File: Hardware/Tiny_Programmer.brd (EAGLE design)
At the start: 59.7 x 15.2 mm, 31 parts, among them Q1 16MHz, U1 ATTINY84, X1 USB-A-H

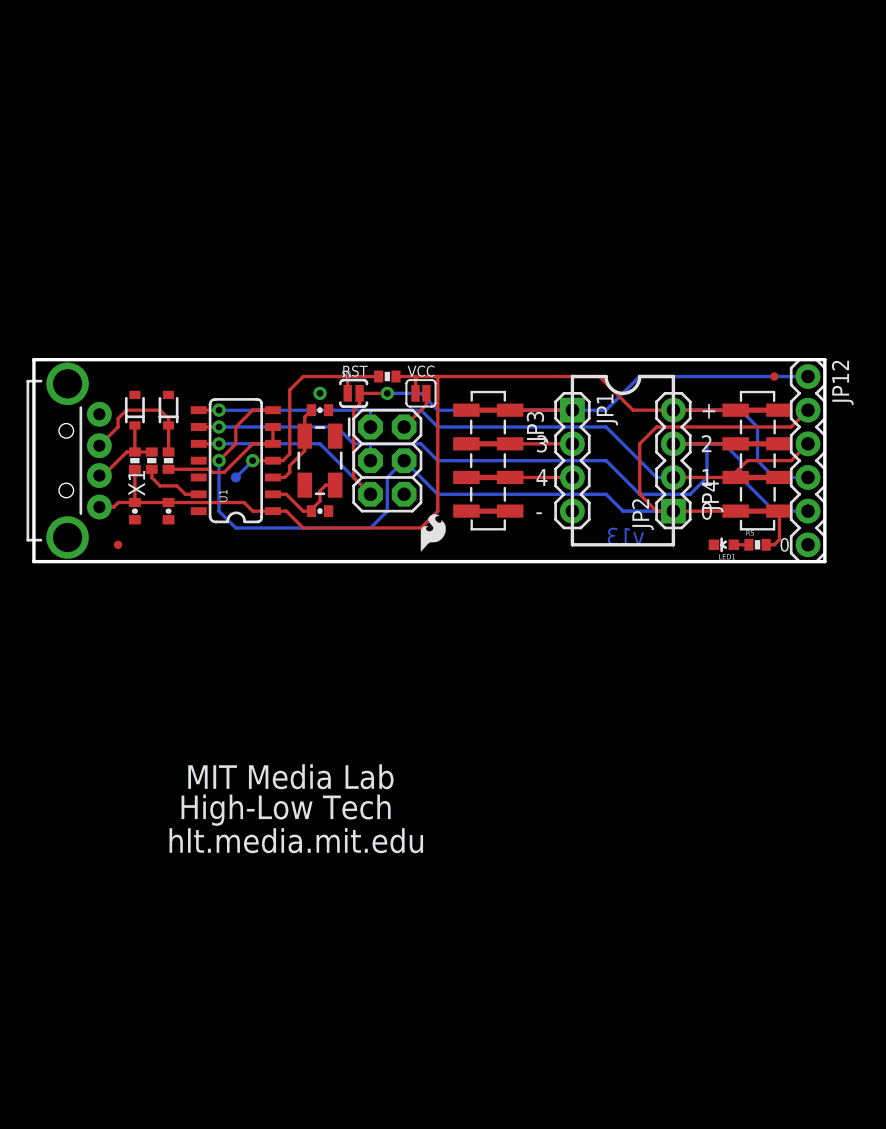
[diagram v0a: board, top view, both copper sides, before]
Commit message: Removed ATTINY85 socket & headers.  Replaced USB A plug with USB Micro B socket.  Shrinkified board layout.  Added shrouded 6-pin ISP header.
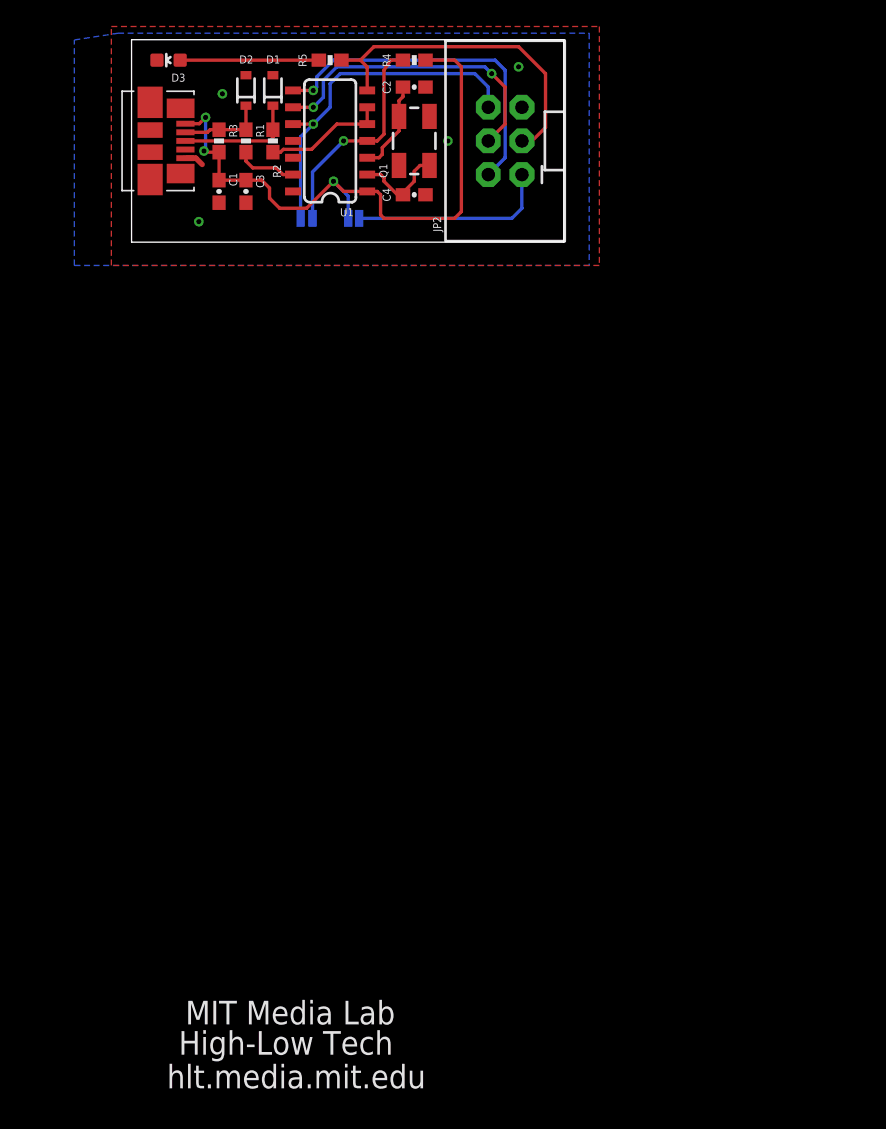
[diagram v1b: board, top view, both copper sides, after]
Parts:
- removed JP11, JP6: LOGO-SFESK, SparkFun-Aesthetics:SFE-LOGO-FLAME
- removed JP12: (no value), SparkFun-Connectors:1X06
- removed JP3, JP4: (no value), SparkFun-Connectors:1X04_SMD_STRAIGHT_COMBO
- removed JP5: LOGO-SFENW2, SparkFun-Aesthetics:SFE-NEW-WEB
- removed JP7, JP8: FIDUCIALUFIDUCIAL, SparkFun:MICRO-FIDUCIAL
- removed JP9: (no value), SparkFun-Connectors:2X3
- removed LED1: Yellow, SparkFun-LED:LED-0603
- removed TP1: TEST-POINT3, SparkFun-Passives:PAD.03X.03
- removed X1: USB-A-H, SparkFun-Connectors:USB-A-H
- added D3: Yellow, SparkFun-LED:LED-0603
- C1, C2, C3, C4: device SparkFun-Passives:0402-CAP -> SparkFun-Capacitors:0603-CAP
- JP1: device SparkFun-Connectors:1X04 -> Molex-47346-0001:MOLEX_47346-0001
- JP2: value (none) -> M03X2-SHROUDED; device SparkFun-Connectors:1X04 -> Darryl:2X3-SHROUDED-B
- R1, R2, R3, R4, R5: device SparkFun-Passives:0402-RES -> SparkFun-Resistors:0603-RES
- moved R5 48.8 mm to (22.4, 37.8)
- moved U$1 39.1 mm to (10.2, 26.5)
- moved JP1 35.6 mm to (11.4, 31.8)
- moved JP2 30.7 mm to (35.6, 31.8)
- moved D2 25.5 mm to (16.0, 35.6)
- moved C2 25.4 mm to (28.7, 35.8)
- moved D1 25.4 mm to (18.0, 35.6)
- moved R2 25.4 mm to (18.0, 31.8)
- moved Q1 25.2 mm to (28.7, 31.8)
- moved R1 25.2 mm to (16.0, 31.8)
- moved U1 25.2 mm to (22.4, 31.8)
- moved C1 25.0 mm to (14.0, 27.9)
- moved R3 25.0 mm to (14.0, 31.8)
- moved C4 24.9 mm to (28.7, 27.7)
- moved C3 24.8 mm to (16.0, 27.9)
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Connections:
- removed net 2: JP1.2, JP3.2
- removed net 3: JP1.3, JP3.3
- removed net N$1: D2.1, R1.1, R3.1, X1.D-
- removed net N$2: D1.1, R2.1, X1.D+
- new net USBDM: D2.1, JP1.2, R1.1, R3.1
- new net USBSP: D1.1, JP1.3, R2.1
- net GND: now also D3.C, JP1.5, JP2.5; no longer JP1.4, JP12.6, JP3.4, JP9.6, LED1.C, X1.GND
- net MISO: no longer JP12.3, JP4.2, JP9.1
- net MOSI: now also JP2.3; no longer JP12.2, JP2.1, JP4.1, JP9.4
- net N$5: now also D3.A; no longer LED1.A
- net RESET: no longer TP1.P$1
- net RST: now also JP2.6; no longer JP1.1, JP12.1, JP3.1, JP9.5
- net SCK: now also JP2.4; no longer JP12.5, JP2.3, JP4.3, JP9.3
- net VCC: now also JP1.1; no longer JP12.4, JP2.4, JP4.4, X1.VBUS
- net VCC': now also JP2.1; no longer JP9.2
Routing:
- net MOSI: track 82.5 -> 25.4 mm, vias 1 -> 0
- net SCK: track 65.8 -> 23.2 mm, vias 1 -> 2
- net RST: track 66.3 -> 26.8 mm, vias 2 -> 1
- net VCC: track 81.5 -> 47.7 mm, vias 0 -> 3
- net MISO: track 50.6 -> 26.1 mm
- net VCC': track 3.24 -> 15.1 mm
- net N$2: track 9.49 -> 0.00 mm
- net N$5: track 1.14 -> 10.5 mm
- net USBSP: track 0.00 -> 9.12 mm
- net 3: track 8.00 -> 0.00 mm
- net N$1: track 6.70 -> 0.00 mm
- net USBDM: track 0.00 -> 6.46 mm
- net 2: track 4.70 -> 0.00 mm
- net GND: track 0.00 -> 1.47 mm, vias 1 -> 4
- net RESET: track 18.1 -> 16.7 mm
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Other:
- board size 59.7 x 15.2 mm -> 32.6 x 15.3 mm
- board text added: "Tinier Programmer"
- board text removed: "+"
- board text removed: "-"
- board text removed: "0"
- board text removed: "1"
- board text removed: "2"
- board text removed: "3"
- board text removed: "4"
- board text removed: "GND"
- board text removed: "ISP"
- board text removed: "Tiny Programmer"
- board text removed: "v13"
